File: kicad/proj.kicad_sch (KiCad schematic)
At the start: 65 parts, among them J1 USB-C, J2 OLED, J3 USB-A, SW1 SW_DIP_x01, SW10 SW_DIP_x01, SW11 SW_DIP_x01, SW12 SW_DIP_x01, SW13 SW_DIP_x01, SW14 SW_DIP_x01, SW15 SW_DIP_x01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

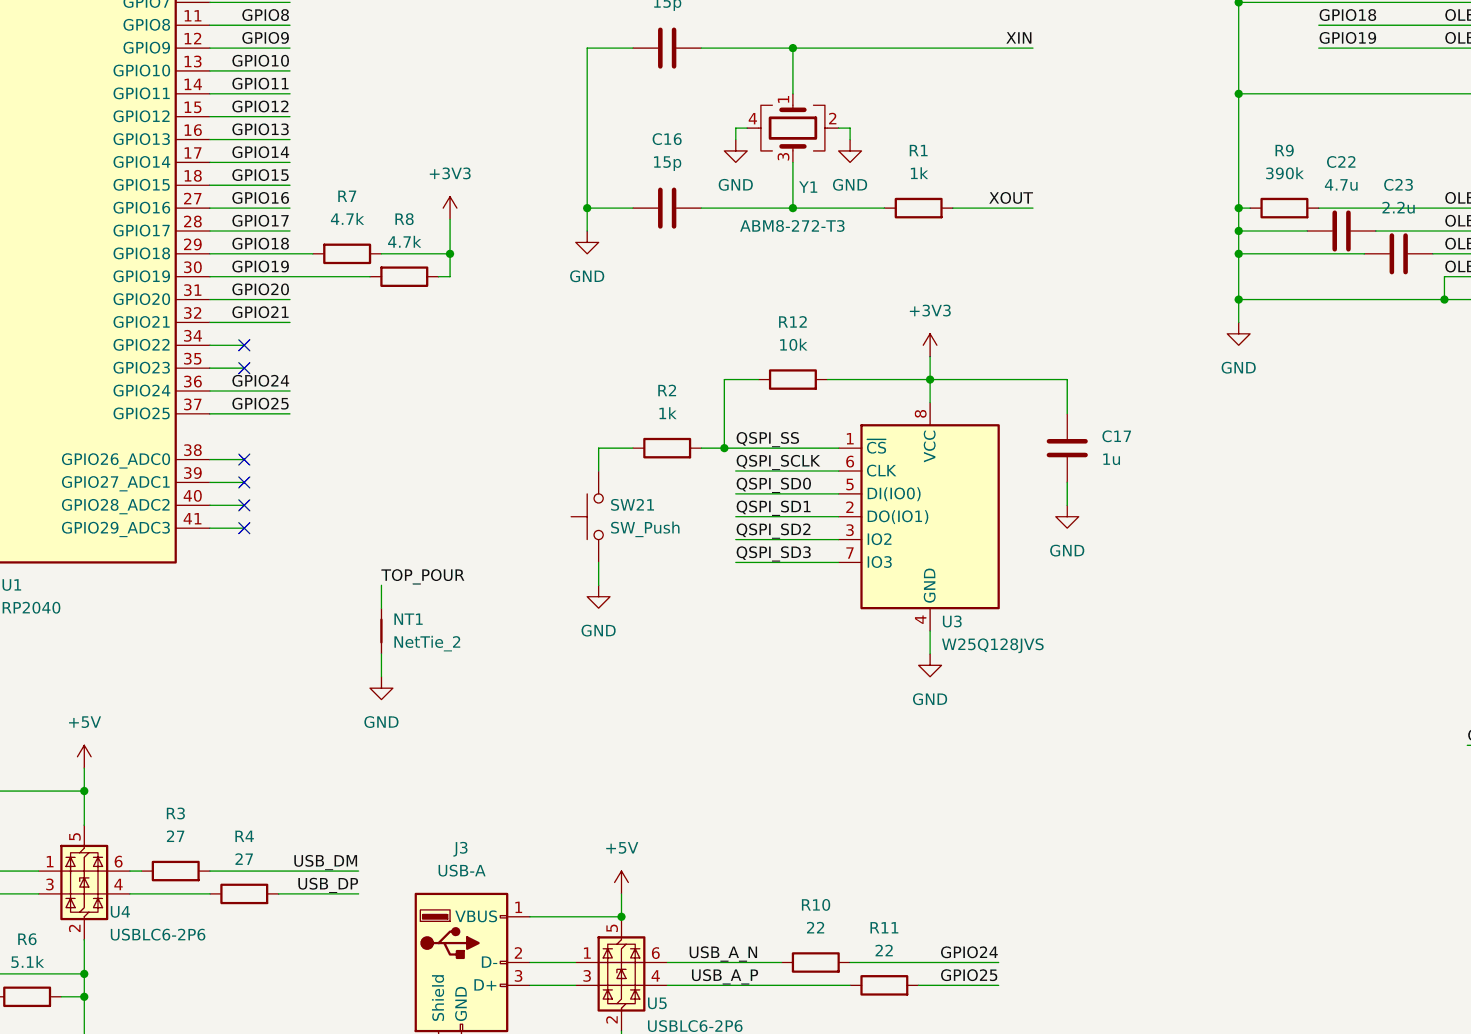
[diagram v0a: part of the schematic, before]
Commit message: adapt for LCSC part numbers
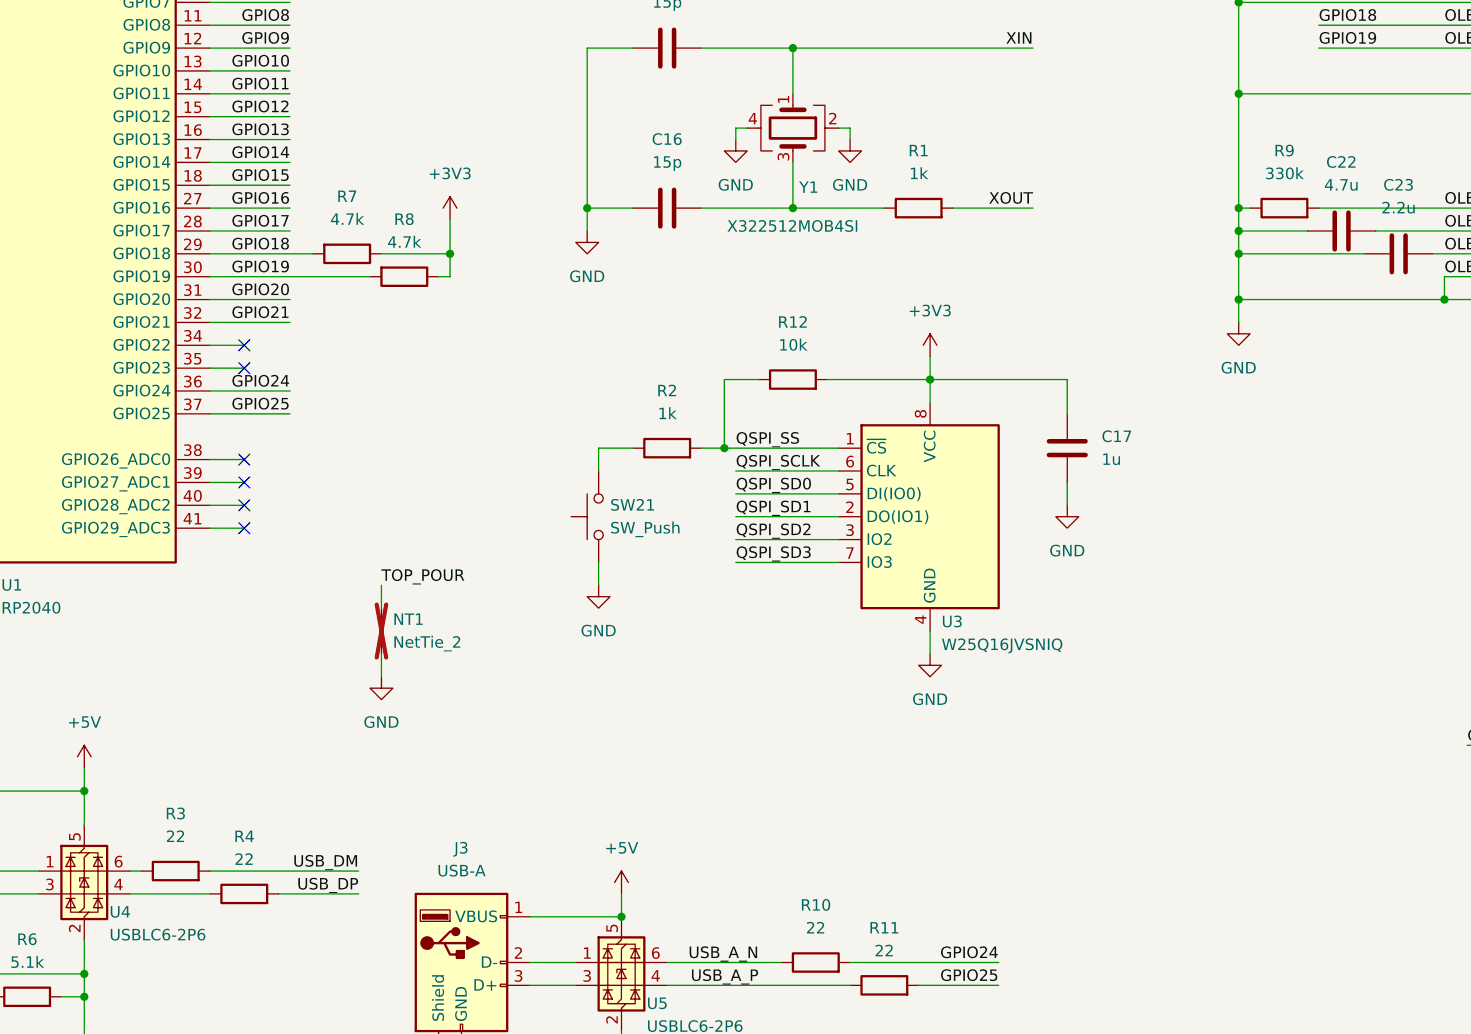
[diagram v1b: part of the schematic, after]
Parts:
- C1, C10, C11, C2, C5, C6, C7, C8, C9: LCSC (none) -> C1525
- C12, C14: LCSC (none) -> C15850
- C15, C16: LCSC (none) -> C1548
- C17, C18, C19, C20, C21, C3, C4: LCSC (none) -> C52923
- C22: LCSC (none) -> C1779
- C23: LCSC (none) -> C377773
- J1: LCSC (none) -> C319148
- J2: LCSC (none) -> C2915410
- J3: LCSC (none) -> C6331170
- NT1: now not fitted
- R1, R2: LCSC (none) -> C11702
- R10, R11: LCSC (none) -> C25092
- R12: LCSC (none) -> C25744
- R3, R4: value 27 -> 22; LCSC (none) -> C25092
- R5, R6: LCSC (none) -> C25905
- R7, R8: LCSC (none) -> C25900
- R9: value 390k -> 330k; LCSC (none) -> C25104
- SW1, SW10, SW11, SW12, SW13, SW14, SW15, SW16, SW17, SW18, SW2, SW3, SW4, SW5, SW6, SW7, SW8, SW9: LCSC (none) -> C5333465
- SW19, SW20: LCSC (none) -> C589295
- SW21: LCSC (none) -> C470427
- U1: LCSC (none) -> C2040
- U2: LCSC (none) -> C51118
- U3: value W25Q128JVS -> W25Q16JVSNIQ; LCSC (none) -> C2456211
- U4, U5: LCSC (none) -> C15999
- Y1: value ABM8-272-T3 -> X322512MOB4SI; LCSC (none) -> C70565

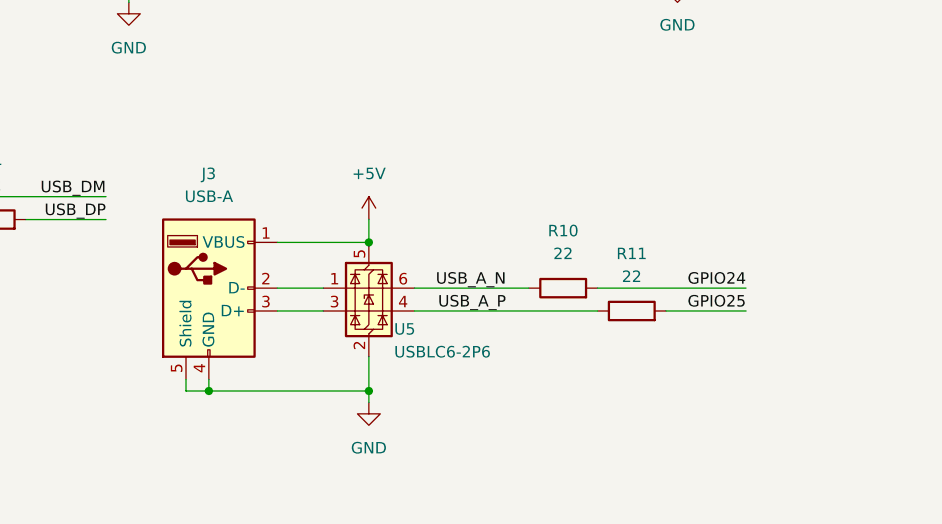
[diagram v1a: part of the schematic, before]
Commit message: replace USB-A with top mount part
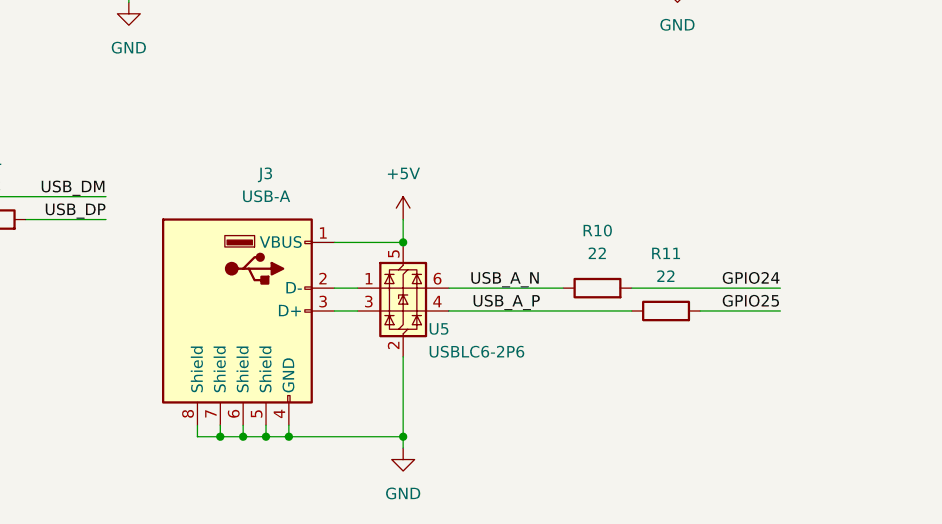
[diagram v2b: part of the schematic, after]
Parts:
- J3: footprint proj:USB-A-SMD_8-5-CB1-9ZB -> proj:USB-A-SMD_USB-M-21
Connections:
- net GND: now also J3.6 (Shield), J3.7 (Shield), J3.8 (Shield)
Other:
- moved on the sheet: R10, R11, U5

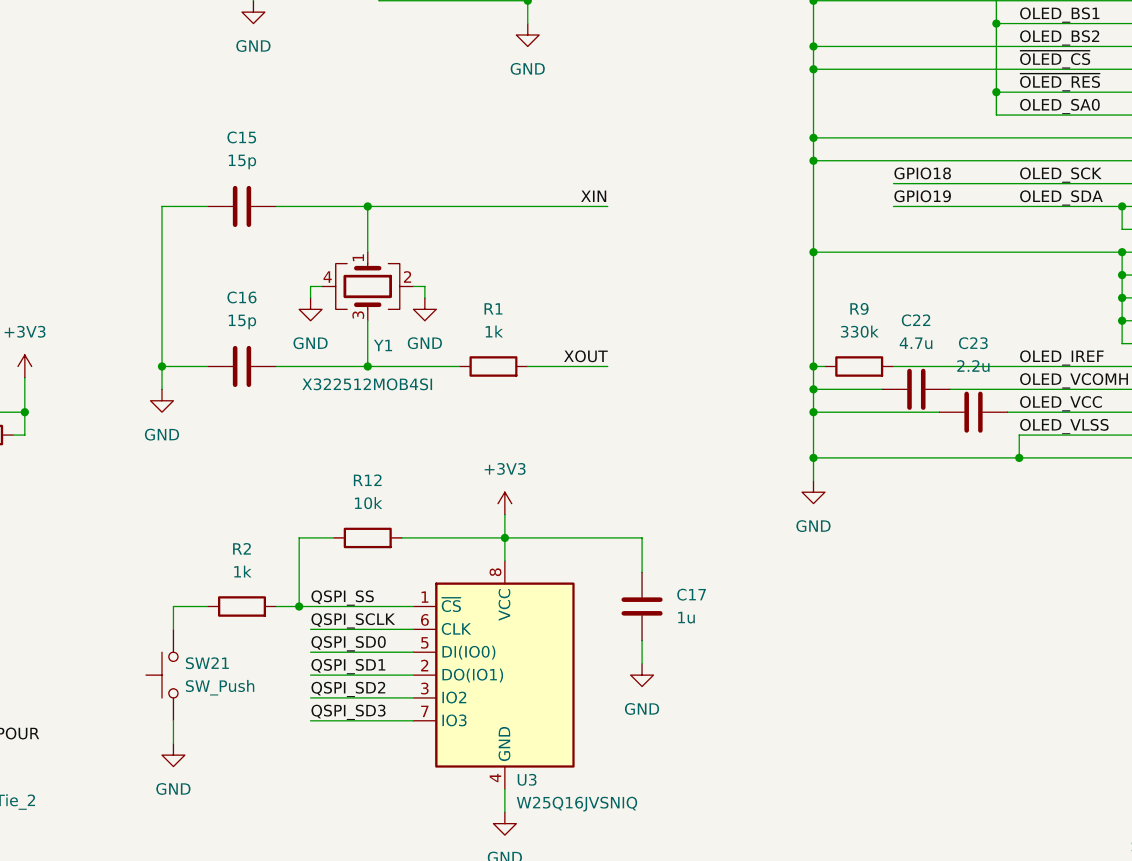
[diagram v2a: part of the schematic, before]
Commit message: add acrylic layouts
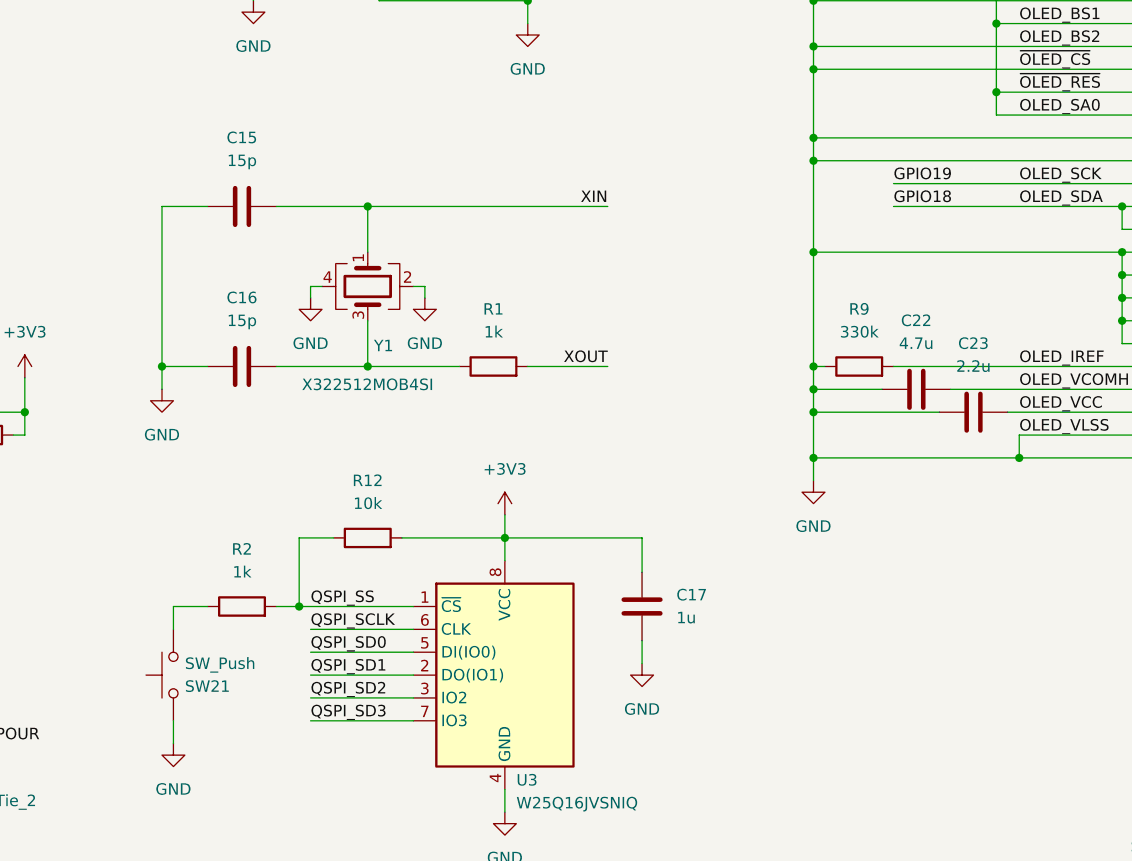
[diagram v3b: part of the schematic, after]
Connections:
- net GND: now also SW21.2; no longer SW21.1
- net GPIO18: now also J2.19 (Pin_19), J2.20 (Pin_20); no longer J2.18 (Pin_18)
- net GPIO19: now also J2.18 (Pin_18); no longer J2.19 (Pin_19), J2.20 (Pin_20)
- net at R2.1: now also SW21.1; no longer SW21.2
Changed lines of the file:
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@@
 		)
 	)
-	(label "GPIO19"
+	(label "GPIO18"
 		(at 201.93 71.12 0)
 		(fields_autoplaced yes)
@@
 		)
 	)
-	(label "GPIO18"
+	(label "GPIO19"
 		(at 201.93 68.58 0)
 		(fields_autoplaced yes)
@@
 		(lib_id "Switch:SW_Push")
 		(at 121.92 123.19 90)
+		(mirror x)
 		(unit 1)
 		(exclude_from_sim no)
@@
 		(on_board yes)
 		(dnp no)
-		(fields_autoplaced yes)
 		(property "Reference" "SW21"
-			(at 123.19 121.9199 90)
+			(at 123.19 124.4601 90)
 			(effects
 				(font
@@
 		)
 		(property "Value" "SW_Push"
-			(at 123.19 124.4599 90)
+			(at 123.19 121.9201 90)
 			(effects
 				(font
